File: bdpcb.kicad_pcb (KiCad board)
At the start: 2 copper layers, 285.8 x 114.3 mm, 292 parts, among them K1 KEYSW, K10 KEYSW, K11 KEYSW, K12 KEYSW, K13 KEYSW, K14 KEYSW, K15 KEYSW, K16 KEYSW, K17 KEYSW, K18 KEYSW, K19 KEYSW, K2 KEYSW, K20 KEYSW, K21 KEYSW, K22 KEYSW, K23 KEYSW, K24 KEYSW, K25 KEYSW, K26 KEYSW, K27 KEYSW, K28 KEYSW, K29 KEYSW, K3 KEYSW, K30 KEYSW, K31 KEYSW, K32 KEYSW, K33 KEYSW, K34 KEYSW, K35 KEYSW, K36 KEYSW, K37 KEYSW, K38 KEYSW, K39 KEYSW, K4 KEYSW, K40 KEYSW, K41 KEYSW, K42 KEYSW, K43 KEYSW, K44 KEYSW, K45 KEYSW, K46 KEYSW, K47 KEYSW, K48 KEYSW, K49 KEYSW, K5 KEYSW, K50 KEYSW, K51 KEYSW, K52 KEYSW, K53 KEYSW, K54 KEYSW, K55 KEYSW, K56 KEYSW, K57 KEYSW, K58 KEYSW, K59 KEYSW, K6 KEYSW, K60 KEYSW, K61 KEYSW, K62 KEYSW, K63 KEYSW, K64 KEYSW, K65 KEYSW, K66 KEYSW, K67 KEYSW, K68 KEYSW, K69 KEYSW, K7 KEYSW, K70 KEYSW, K71 KEYSW, K72 KEYSW, K73 KEYSW, K74 KEYSW, K75 KEYSW, K76 KEYSW, K77 KEYSW, K78 KEYSW, K79 KEYSW, K8 KEYSW, K80 KEYSW, K81 KEYSW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

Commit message: two rows of diodes
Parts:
- moved TP4 5.02 mm to (149.1, 54.4)
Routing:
- net LA_C: track 0.00 -> 290.6 mm
- net LA_F: track 0.00 -> 290.6 mm
- net LA_B: track 0.00 -> 290.5 mm
- net LA_E: track 0.00 -> 290.5 mm
- net row1: track 57.2 -> 274.0 mm
- net LA_A: track 0.00 -> 44.2 mm, vias 0 -> 5
- net Net-(D28-Pad2): track 0.00 -> 4.30 mm
- net Net-(D27-Pad2): track 0.00 -> 4.30 mm
- net Net-(D30-Pad2): track 0.00 -> 4.30 mm
- net Net-(D29-Pad2): track 0.00 -> 4.30 mm
- net Net-(D26-Pad2): track 0.00 -> 4.30 mm
- net Net-(D25-Pad2): track 0.00 -> 4.30 mm
- net Net-(D24-Pad2): track 0.00 -> 4.30 mm
- net Net-(D23-Pad2): track 0.00 -> 4.30 mm
- net Net-(D22-Pad2): track 0.00 -> 4.03 mm
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
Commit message: more diode routing
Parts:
- moved D44 14.1 mm to (293.7, 57.9), turned to 270 degrees
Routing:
- net LA_D: track 0.00 -> 324.1 mm, vias 0 -> 41
- net LA_A: track 44.2 -> 324.1 mm, vias 5 -> 41
- net col0: track 4.86 -> 108.0 mm
- net col14: track 0.00 -> 103.0 mm
- net col13: track 0.00 -> 74.7 mm
- net col1: track 0.00 -> 48.0 mm
- net col6: track 0.00 -> 23.4 mm
- net col5: track 0.00 -> 22.1 mm
- net col9: track 0.00 -> 22.0 mm
- net col8: track 0.00 -> 22.0 mm
- net col7: track 0.00 -> 22.0 mm
- net col2: track 0.00 -> 22.0 mm
- net col12: track 0.00 -> 22.0 mm
- net col10: track 0.00 -> 22.0 mm
- net col3: track 0.00 -> 22.0 mm
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
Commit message: good progress on traces
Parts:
- moved D77 20.8 mm to (174.6, 115.1), turned to 270 degrees
- moved D57 20.0 mm to (286.5, 77.0), turned to 270 degrees
- moved D51 15.5 mm to (160.3, 77.0), turned to 270 degrees
- moved D65 15.5 mm to (184.2, 96.0), turned to 270 degrees
- moved D69 15.5 mm to (260.4, 96.0), turned to 270 degrees
- moved D33 15.5 mm to (79.4, 57.9), turned to 270 degrees
- moved D46 15.5 mm to (65.1, 77.0), turned to 270 degrees
- moved D48 15.5 mm to (103.2, 77.0), turned to 270 degrees
- moved D60 15.5 mm to (88.9, 96.0), turned to 270 degrees
- moved D75 15.5 mm to (112.7, 115.1), turned to 270 degrees
- moved D58 15.5 mm to (41.3, 96.0), turned to 270 degrees
- moved D55 15.5 mm to (236.5, 77.0), turned to 270 degrees
- moved D66 15.5 mm to (203.2, 96.0), turned to 270 degrees
- moved D70 15.5 mm to (279.4, 96.0), turned to 270 degrees
- moved D71 15.5 mm to (298.4, 96.0), turned to 270 degrees
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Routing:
- net LB_H: track 0.00 -> 286.9 mm
- net LB_I: track 0.00 -> 283.2 mm
- net LA_I: track 0.00 -> 279.3 mm
- net LA_H: track 0.00 -> 279.3 mm
- net row5: track 0.00 -> 268.5 mm
- net LB_E: track 0.00 -> 249.0 mm
- net row3: track 0.00 -> 222.8 mm
- net LB_B: track 0.00 -> 219.7 mm
- net LB_C: track 0.00 -> 219.5 mm
- net row2: track 0.00 -> 219.1 mm
- net LB_F: track 0.00 -> 196.3 mm
- net LA_G: track 0.00 -> 166.8 mm, vias 0 -> 20
- net LB_D: track 0.00 -> 160.7 mm, vias 0 -> 20
- net row4: track 0.00 -> 133.3 mm
- net col12: track 22.0 -> 118.8 mm
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
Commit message: getting there on traces
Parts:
- moved C10 11.7 mm to (284.8, 145.7)
- moved C11 11.6 mm to (284.8, 150.4)
- moved C5 9.27 mm to (284.8, 135.5)
- moved C3 3.14 mm to (273.0, 136.9)
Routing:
- net LB_G: track 91.5 -> 332.2 mm, vias 11 -> 32
- net LB_A: track 32.7 -> 224.0 mm, vias 2 -> 27
- net LB_D: track 160.7 -> 310.2 mm, vias 20 -> 38
- net LA_G: track 166.8 -> 312.6 mm, vias 20 -> 38
- net row4: track 133.3 -> 232.3 mm
- net col2: track 22.0 -> 106.1 mm
- net LB_F: track 196.3 -> 279.4 mm
- net col5: track 44.0 -> 104.2 mm
- net col1: track 48.0 -> 108.1 mm
- net LB_3: track 0.00 -> 52.8 mm, vias 0 -> 3
- net LA_7: track 0.00 -> 52.8 mm, vias 0 -> 3
- net LA_3: track 0.00 -> 52.0 mm, vias 0 -> 3
- net LA_9: track 0.00 -> 51.9 mm, vias 0 -> 3
- net LA_11: track 0.00 -> 51.9 mm, vias 0 -> 3
- net LA_2: track 0.00 -> 51.8 mm, vias 0 -> 3
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
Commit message: schleeping
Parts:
- moved R6 202.0 mm to (154.0, -3.43)
- moved R4 197.8 mm to (161.2, -3.56)
- moved R5 191.5 mm to (157.7, -3.56)
- moved C1 185.7 mm to (37.3, 79.7), turned to 90 degrees
- moved C5 174.7 mm to (161.5, 11.8)
- moved JP5 168.9 mm to (139.7, 8.51)
- moved R2 168.2 mm to (116.4, 12.7)
- moved C2 164.7 mm to (175.1, 7.24)
- moved C3 162.4 mm to (169.4, 11.8)
- moved R3 160.6 mm to (112.6, 12.7)
- moved C7 160.4 mm to (153.5, 11.6)
- moved JP6 160.3 mm to (134.8, 8.51)
- moved R1 160.2 mm to (120.0, 12.7)
- moved C6 156.3 mm to (157.8, 11.7)
- moved C8 152.2 mm to (149.3, 11.9)
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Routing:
- net LB_7: track 0.00 -> 26.8 mm, vias 0 -> 2
- net LB_8: track 26.6 -> 49.4 mm, vias 2 -> 3
- net col7: track 42.3 -> 63.4 mm
- net col6: track 64.2 -> 85.2 mm
- net LB_A: track 224.0 -> 241.5 mm, vias 27 -> 28
- net GND: track 0.00 -> 3.52 mm
- net +3V3: track 0.00 -> 3.26 mm
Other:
- net class Default: trace_width 0.25 -> 0.254
- net class Power added: clearance 0.2, trace_width 0.381, via_dia 0.8, via_drill 0.4

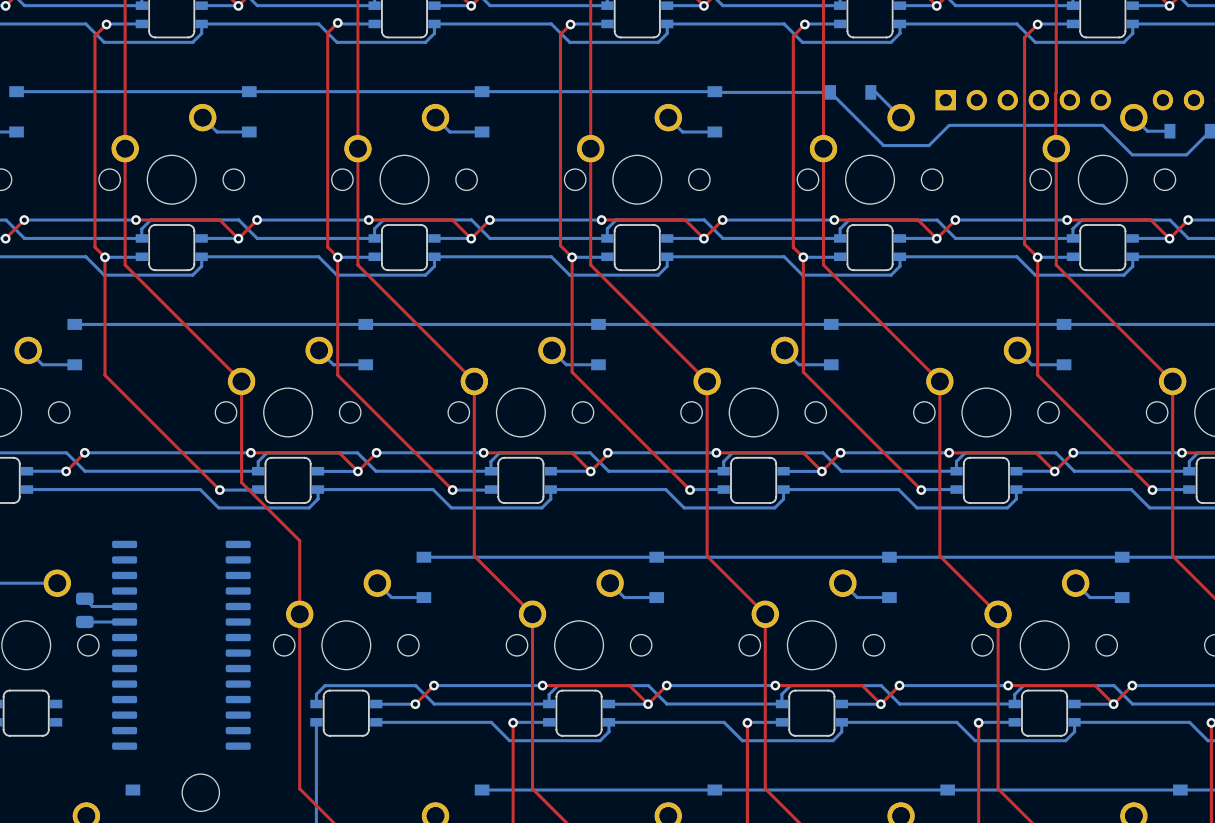
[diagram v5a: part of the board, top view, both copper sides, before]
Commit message: fixed feather footprint pinout to match symbol
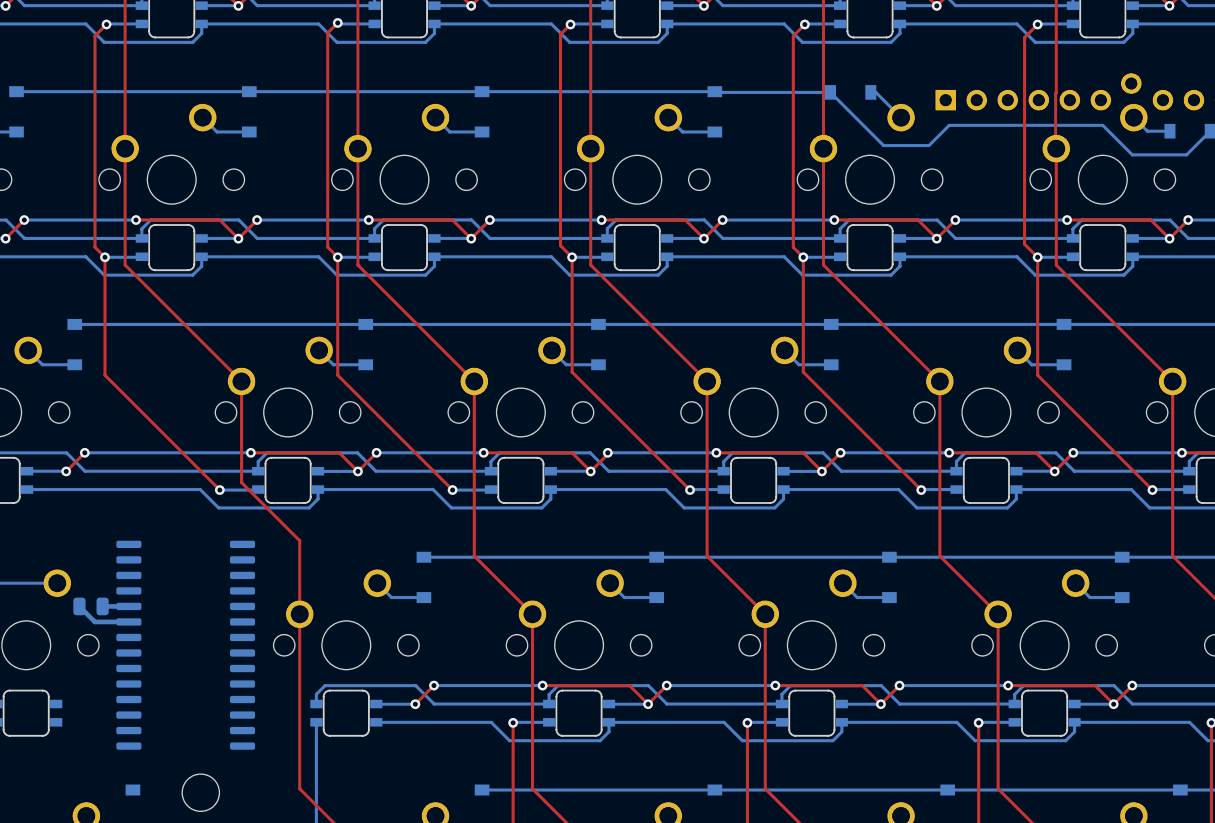
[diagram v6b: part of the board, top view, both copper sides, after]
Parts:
- K76: footprint ai03Footprints:MXOnly-1.25U-NoLED -> ai03Footprints:MXOnly-1U-NoLED
- moved C1 0.60 mm to (37.8, 79.4), turned to 0 degrees
- moved U2 0.35 mm to (45.6, 82.5)
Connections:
- SW1 pad 3: Net-(SW1-Pad3) -> (no net)
- U2 pad 11: Net-(U2-Pad11) -> (no net)
- U2 pad 14: Net-(U2-Pad14) -> (no net)
- U2 pad 19: Net-(U2-Pad19) -> (no net)
- U2 pad 20: Net-(U2-Pad20) -> (no net)
- U2 pad 8: Net-(U2-Pad8) -> (no net)
- U3 pad 1: Net-(U3-Pad1) -> (no net)
- U3 pad 13: Net-(U3-Pad13) -> (no net)
- U3 pad 14: Net-(U3-Pad14) -> (no net)
- U3 pad 15: Net-(U3-Pad15) -> (no net)
- U3 pad 33: Net-(U3-Pad33) -> (no net)
- U3 pad 36: Net-(U3-Pad36) -> (no net)
- U4 pad 1: Net-(U4-Pad1) -> (no net)
- U4 pad 13: Net-(U4-Pad13) -> (no net)
- U4 pad 14: Net-(U4-Pad14) -> (no net)
- U4 pad 15: Net-(U4-Pad15) -> (no net)
- U4 pad 33: Net-(U4-Pad33) -> (no net)
- U4 pad 36: Net-(U4-Pad36) -> (no net)
- U4 pad 45: Net-(U4-Pad45) -> (no net)
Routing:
- net GND: track 3.52 -> 2.15 mm
- net +3V3: track 3.26 -> 4.57 mm

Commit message: bottom rows, still cant track to qfn pins
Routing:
- net col13: track 71.7 -> 335.7 mm, vias 0 -> 3
- net col14: track 103.0 -> 358.2 mm
- net col7: track 63.4 -> 107.4 mm
- net LA_8: track 25.5 -> 51.5 mm, vias 2 -> 3

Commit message: random stuff; power switch, some cols, re-added accidentally deleted key
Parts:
- moved TP3 75.0 mm to (80.2, 19.1)
- moved SW1 71.1 mm to (72.4, 21.1), turned to 180 degrees
- moved TP2 48.7 mm to (55.6, 20.6)
- moved C1 16.9 mm to (53.5, 85.7), turned to 180 degrees
- moved JP1 16.7 mm to (20.7, 80.6), turned to 90 degrees
- moved JP2 15.8 mm to (20.7, 85.3), turned to 90 degrees
- moved JP3 15.1 mm to (20.7, 90.0), turned to 90 degrees
- moved D3 7.94 mm to (61.9, 19.8), turned to 0 degrees
- moved D46 1.59 mm to (65.1, 78.6), turned to 90 degrees
- moved D47 1.59 mm to (84.1, 78.6), turned to 90 degrees
- moved D48 1.59 mm to (103.2, 78.6), turned to 90 degrees
- moved D49 1.59 mm to (122.2, 78.6), turned to 90 degrees
- moved D50 1.59 mm to (141.3, 78.6), turned to 90 degrees
- moved D51 1.59 mm to (160.3, 78.6), turned to 90 degrees
- moved D52 1.59 mm to (179.4, 78.6), turned to 90 degrees
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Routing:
- net col12: track 109.9 -> 332.1 mm, vias 0 -> 1
- net col11: track 103.1 -> 295.9 mm, vias 0 -> 1
- net col10: track 103.1 -> 277.2 mm, vias 0 -> 1
- net col9: track 103.1 -> 258.4 mm, vias 0 -> 1
- net col8: track 103.1 -> 239.7 mm, vias 0 -> 1
- net col2: track 106.1 -> 163.8 mm
- net row3: track 222.8 -> 279.8 mm, vias 0 -> 2
- net GND: track 2.15 -> 58.2 mm, vias 0 -> 1
- net Net-(SW1-Pad1): track 0.00 -> 50.0 mm
- net col13: track 335.7 -> 299.4 mm, vias 3 -> 1
- net col1: track 108.1 -> 134.8 mm, vias 0 -> 1
- net Net-(JP3-Pad2): track 0.00 -> 24.8 mm
- net Net-(JP1-Pad2): track 0.00 -> 23.4 mm
- net Net-(JP2-Pad2): track 0.00 -> 23.2 mm
- net col0: track 108.0 -> 121.5 mm
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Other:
- net class Default: trace_width 0.254 -> 0.25
